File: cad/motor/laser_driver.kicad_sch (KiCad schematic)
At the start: 8 parts, among them Q1 NMOS, U1 ${SIM.PARAMS}

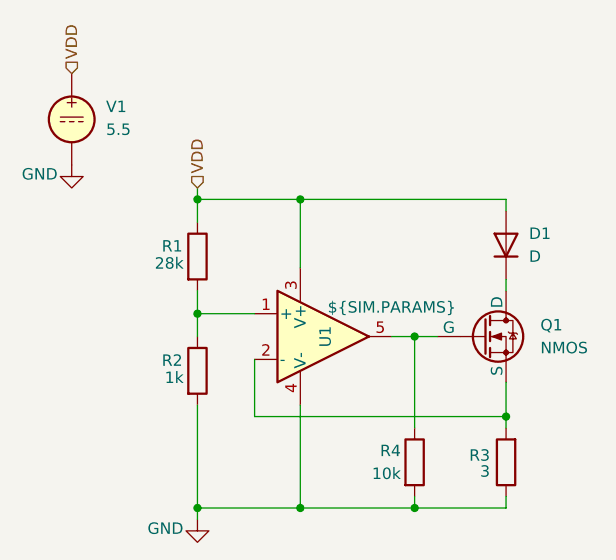
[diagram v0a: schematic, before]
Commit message: update galvo + laser driver
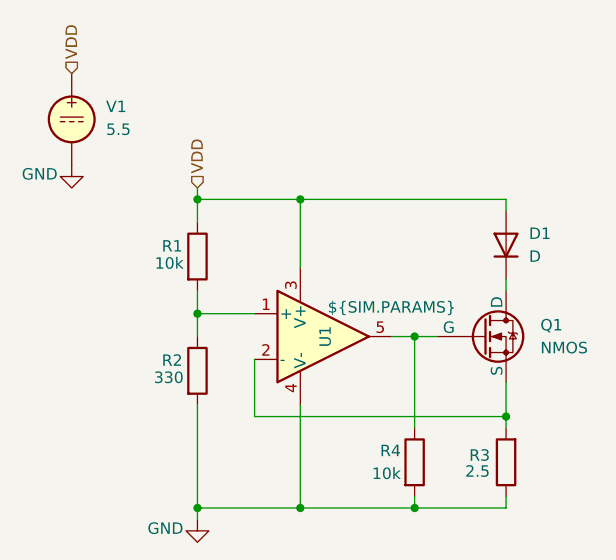
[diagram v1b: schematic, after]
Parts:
- R1: value 28k -> 10k
- R2: value 1k -> 330
- R3: value 3 -> 2.5
